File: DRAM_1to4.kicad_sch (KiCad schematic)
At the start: 1 part, among them U1 K4A8G085WC-BCPB

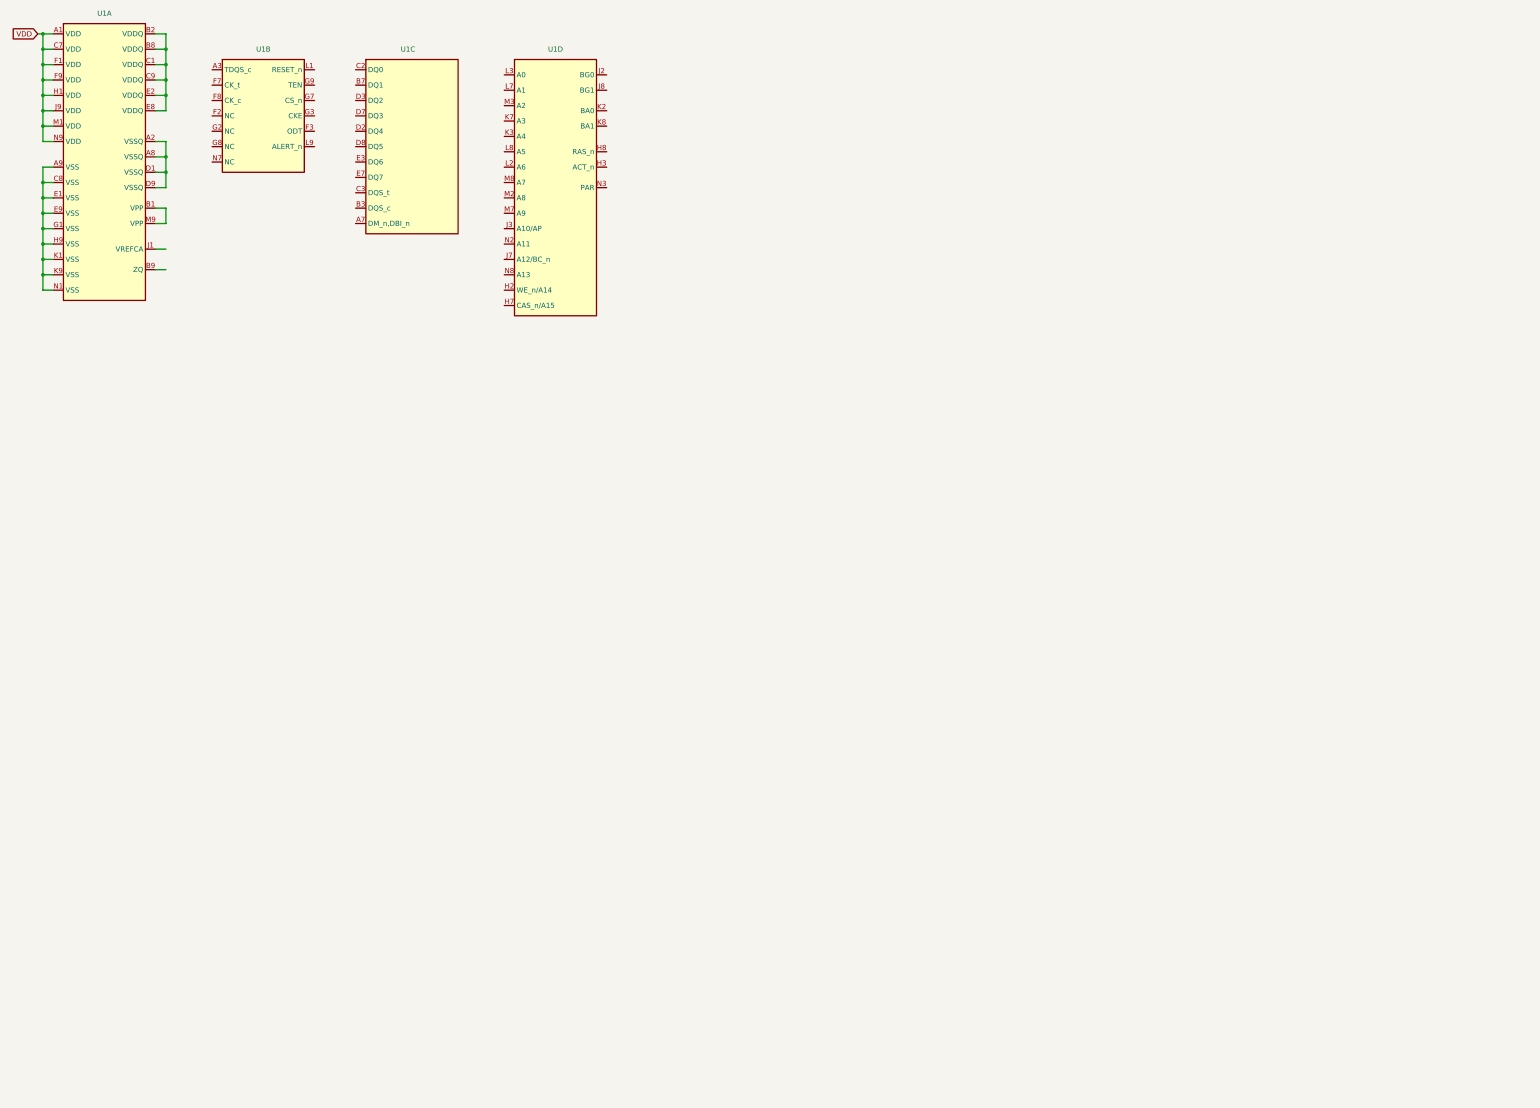
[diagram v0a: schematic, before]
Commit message: Update schametic 1. Adding 7 DRAMS, 2. Replacing a SPD EEPROM with new one that is including in a temperature sensor, 3. modifying a DIMM Connector and DRAM PAD
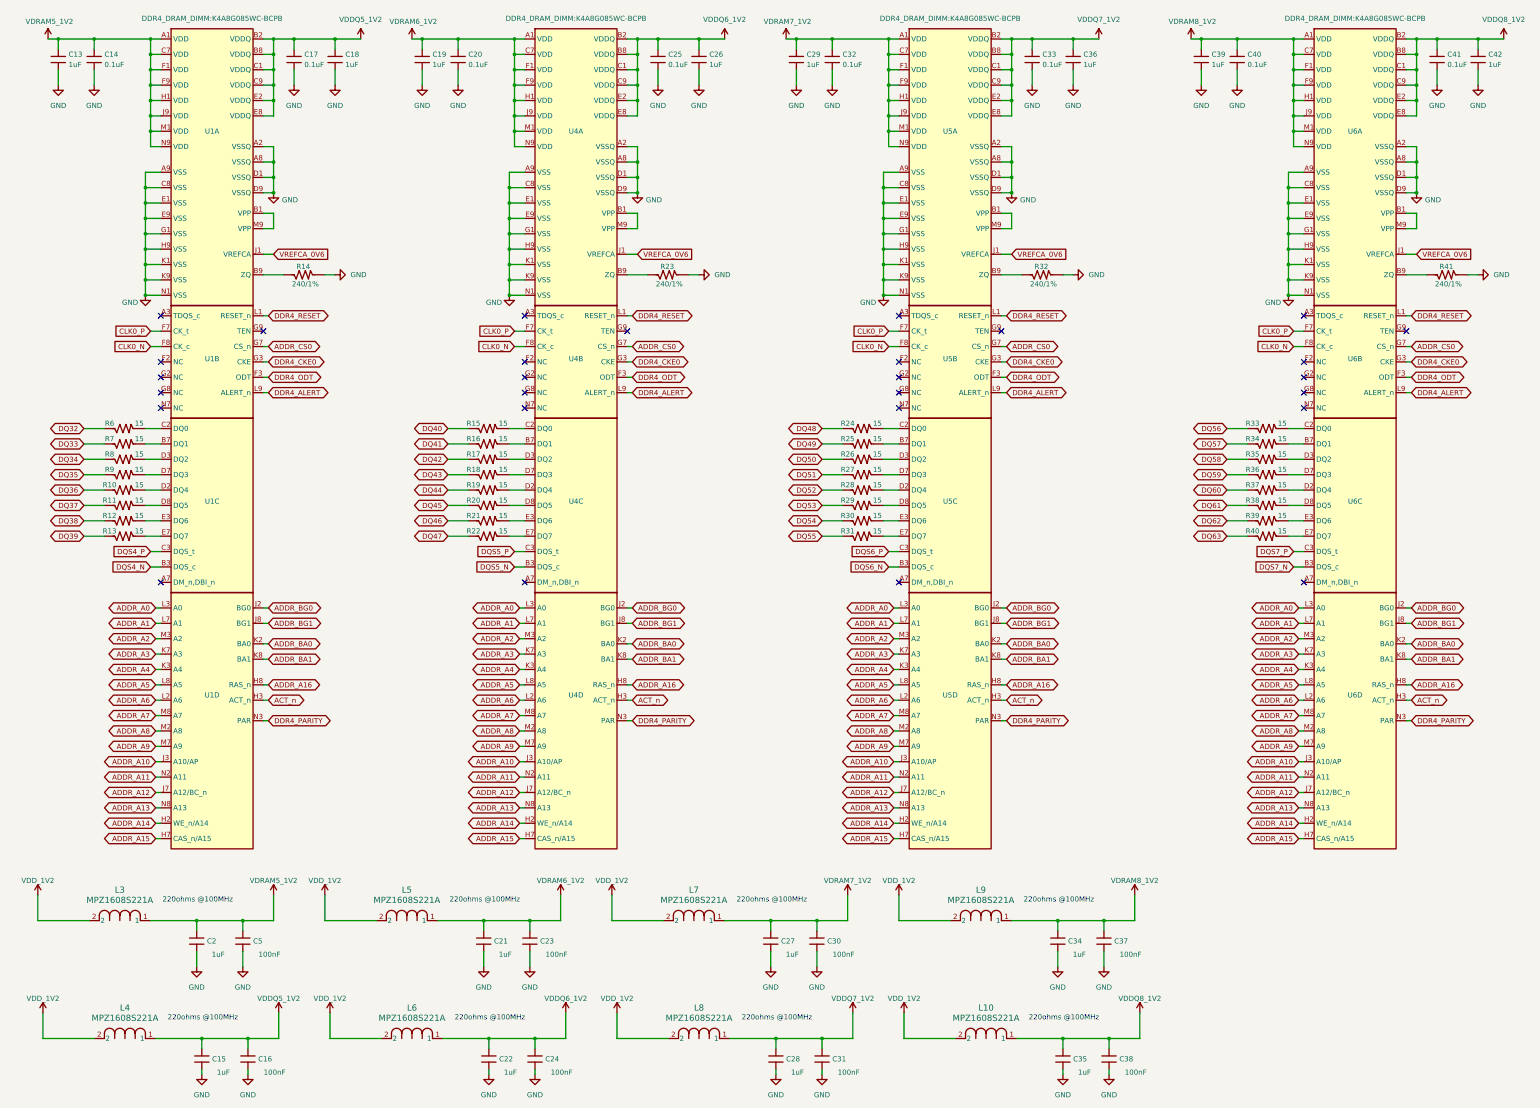
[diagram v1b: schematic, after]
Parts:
- removed U1: K4A8G085WC-BCPB, DDR4_DRAM_DIMM:K4A8G085WC-BCPB, symbol DDR4_DRAM_DIMM:K4A8G085WC-BCPB
- added C13, C18, C19, C26, C29, C36, C39, C42: 1uF, Capacitor_SMD:C_0402_1005Metric_Pad0.74x0.62mm_HandSolder, symbol Mixed_signal:CAP_1608
- added C14, C17, C20, C25, C32, C33, C40, C41: 0.1uF, Capacitor_SMD:C_0402_1005Metric_Pad0.74x0.62mm_HandSolder, symbol Mixed_signal:CAP_1608
- added C15, C2, C21, C22, C27, C28, C34, C35: 1uF, Capacitor_SMD:C_01005_0402Metric_Pad0.57x0.30mm_HandSolder, symbol Mixed_signal:CAP_1005
- added C16, C23, C24, C30, C31, C37, C38, C5: 100nF, Capacitor_SMD:C_01005_0402Metric_Pad0.57x0.30mm_HandSolder, symbol Mixed_signal:CAP_1005
- added L10, L3, L4, L5, L6, L7, L8, L9: MPZ1608S221A, DDR4_DRAM_DIMM:MPZ1608S260ATAH0, symbol MPZ1608S260ATAH0:MPZ1608S221A
- added R10, R11, R12, R13, R15, R16, R17, R18, R19, R20, R21, R22, R24, R25, R26, R27, R28, R29, R30, R31, R33, R34, R35, R36, R37, R38, R39, R40, R6, R7, R8, R9: 15, Capacitor_SMD:C_0402_1005Metric_Pad0.74x0.62mm_HandSolder, symbol Mixed_signal:RES_1005
- added R14, R23, R32, R41: 240/1%, Capacitor_SMD:C_0402_1005Metric_Pad0.74x0.62mm_HandSolder, symbol Mixed_signal:RES_1005
- added U1, U4, U5, U6: K4A8G085WC-BCPB, DDR4_DRAM_DIMM:K4A8G085WC-BCPB, symbol DDR4_DIMM:K4A8G085WC-BCPB
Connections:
- new net: R7.2, U1.B7 (DQ1)
- new net: R6.2, U1.C2 (DQ0)
- new net: R10.2, U1.D2 (DQ4)
- new net: R8.2, U1.D3 (DQ2)
- new net: R9.2, U1.D7 (DQ3)
- new net: R11.2, U1.D8 (DQ5)
- new net: R12.2, U1.E3 (DQ6)
- new net: R13.2, U1.E7 (DQ7)
- new net: R16.2, U4.B7 (DQ1)
- new net: R29.2, U5.D8 (DQ5)
- new net: R27.2, U5.D7 (DQ3)
- new net: R34.2, U6.B7 (DQ1)
- new net: R18.2, U4.D7 (DQ3)
- new net: U1.B1 (VPP), U1.M9 (VPP)
- new net: R14.1, U1.B9 (ZQ)
- new net: R39.2, U6.E3 (DQ6)
- new net: R40.2, U6.E7 (DQ7)
- new net: R26.2, U5.D3 (DQ2)
- new net: R19.2, U4.D2 (DQ4)
- new net: R24.2, U5.C2 (DQ0)
- new net: R25.2, U5.B7 (DQ1)
- new net: R28.2, U5.D2 (DQ4)
- new net: R30.2, U5.E3 (DQ6)
- new net: R31.2, U5.E7 (DQ7)
- new net: R32.1, U5.B9 (ZQ)
- new net: R37.2, U6.D2 (DQ4)
- new net: R15.2, U4.C2 (DQ0)
- new net: R17.2, U4.D3 (DQ2)
- new net: R20.2, U4.D8 (DQ5)
- new net: R21.2, U4.E3 (DQ6)
- new net: R22.2, U4.E7 (DQ7)
- new net: U5.B1 (VPP), U5.M9 (VPP)
- new net: R38.2, U6.D8 (DQ5)
- new net: R35.2, U6.D3 (DQ2)
- new net: R41.1, U6.B9 (ZQ)
- new net: R33.2, U6.C2 (DQ0)
- new net: R23.1, U4.B9 (ZQ)
- new net: R36.2, U6.D7 (DQ3)
- new net: U4.B1 (VPP), U4.M9 (VPP)
- new net: U6.B1 (VPP), U6.M9 (VPP)
- new net ACT_n: U1.H3 (ACT_n), U4.H3 (ACT_n), U5.H3 (ACT_n), U6.H3 (ACT_n)
- new net ADDR_A0: U1.L3 (A0), U4.L3 (A0), U5.L3 (A0), U6.L3 (A0)
- new net ADDR_A1: U1.L7 (A1), U4.L7 (A1), U5.L7 (A1), U6.L7 (A1)
- new net ADDR_A10: U1.J3 (A10/AP), U4.J3 (A10/AP), U5.J3 (A10/AP), U6.J3 (A10/AP)
- new net ADDR_A11: U1.N2 (A11), U4.N2 (A11), U5.N2 (A11), U6.N2 (A11)
- new net ADDR_A12: U1.J7 (A12/BC_n), U4.J7 (A12/BC_n), U5.J7 (A12/BC_n), U6.J7 (A12/BC_n)
- new net ADDR_A13: U1.N8 (A13), U4.N8 (A13), U5.N8 (A13), U6.N8 (A13)
- new net ADDR_A14: U1.H2 (WE_n/A14), U4.H2 (WE_n/A14), U5.H2 (WE_n/A14), U6.H2 (WE_n/A14)
- new net ADDR_A15: U1.H7 (CAS_n/A15), U4.H7 (CAS_n/A15), U5.H7 (CAS_n/A15), U6.H7 (CAS_n/A15)
- new net ADDR_A16: U1.H8 (RAS_n), U4.H8 (RAS_n), U5.H8 (RAS_n), U6.H8 (RAS_n)
- new net ADDR_A2: U1.M3 (A2), U4.M3 (A2), U5.M3 (A2), U6.M3 (A2)
- new net ADDR_A3: U1.K7 (A3), U4.K7 (A3), U5.K7 (A3), U6.K7 (A3)
- new net ADDR_A4: U1.K3 (A4), U4.K3 (A4), U5.K3 (A4), U6.K3 (A4)
- new net ADDR_A5: U1.L8 (A5), U4.L8 (A5), U5.L8 (A5), U6.L8 (A5)
- new net ADDR_A6: U1.L2 (A6), U4.L2 (A6), U5.L2 (A6), U6.L2 (A6)
- new net ADDR_A7: U1.M8 (A7), U4.M8 (A7), U5.M8 (A7), U6.M8 (A7)
- new net ADDR_A8: U1.M2 (A8), U4.M2 (A8), U5.M2 (A8), U6.M2 (A8)
- new net ADDR_A9: U1.M7 (A9), U4.M7 (A9), U5.M7 (A9), U6.M7 (A9)
- new net ADDR_BA0: U1.K2 (BA0), U4.K2 (BA0), U5.K2 (BA0), U6.K2 (BA0)
- new net ADDR_BA1: U1.K8 (BA1), U4.K8 (BA1), U5.K8 (BA1), U6.K8 (BA1)
- new net ADDR_BG0: U1.J2 (BG0), U4.J2 (BG0), U5.J2 (BG0), U6.J2 (BG0)
- new net ADDR_BG1: U1.J8 (BG1), U4.J8 (BG1), U5.J8 (BG1), U6.J8 (BG1)
- new net ADDR_CS0: U1.G7 (CS_n), U4.G7 (CS_n), U5.G7 (CS_n), U6.G7 (CS_n)
- new net CLK0_N: U1.F8 (CK_c), U4.F8 (CK_c), U5.F8 (CK_c), U6.F8 (CK_c)
- new net CLK0_P: U1.F7 (CK_t), U4.F7 (CK_t), U5.F7 (CK_t), U6.F7 (CK_t)
- new net DDR4_ALERT: U1.L9 (ALERT_n), U4.L9 (ALERT_n), U5.L9 (ALERT_n), U6.L9 (ALERT_n)
- new net DDR4_CKE0: U1.G3 (CKE), U4.G3 (CKE), U5.G3 (CKE), U6.G3 (CKE)
- new net DDR4_ODT: U1.F3 (ODT), U4.F3 (ODT), U5.F3 (ODT), U6.F3 (ODT)
- new net DDR4_PARITY: U1.N3 (PAR), U4.N3 (PAR), U5.N3 (PAR), U6.N3 (PAR)
- new net DDR4_RESET: U1.L1 (RESET_n), U4.L1 (RESET_n), U5.L1 (RESET_n), U6.L1 (RESET_n)
- new net DQ32: R6.1
- new net DQ33: R7.1
- new net DQ34: R8.1
- new net DQ35: R9.1
- new net DQ36: R10.1
- new net DQ37: R11.1
- new net DQ38: R12.1
- new net DQ39: R13.1
- new net DQ40: R15.1
- new net DQ41: R16.1
- new net DQ42: R17.1
- new net DQ43: R18.1
- new net DQ44: R19.1
- new net DQ45: R20.1
- new net DQ46: R21.1
- new net DQ47: R22.1
- new net DQ48: R24.1
- new net DQ49: R25.1
- new net DQ50: R26.1
- new net DQ51: R27.1
- new net DQ52: R28.1
- new net DQ53: R29.1
- new net DQ54: R30.1
- new net DQ55: R31.1
- new net DQ56: R33.1
- new net DQ57: R34.1
- new net DQ58: R35.1
- new net DQ59: R36.1
- new net DQ60: R37.1
- new net DQ61: R38.1
- new net DQ62: R39.1
- new net DQ63: R40.1
- new net DQS4_N: U1.B3 (DQS_c)
- new net DQS4_P: U1.C3 (DQS_t)
- new net DQS5_N: U4.B3 (DQS_c)
- new net DQS5_P: U4.C3 (DQS_t)
- new net DQS6_N: U5.B3 (DQS_c)
- new net DQS6_P: U5.C3 (DQS_t)
- new net DQS7_N: U6.B3 (DQS_c)
- new net DQS7_P: U6.C3 (DQS_t)
- new net GND: C13.1, C14.1, C15.1, C16.1, C17.1, C18.1, C19.1, C2.1, C20.1, C21.1, C22.1, C23.1, C24.1, C25.1, C26.1, C27.1, C28.1, C29.1, C30.1, C31.1, C32.1, C33.1, C34.1, C35.1, C36.1, C37.1, C38.1, C39.1, C40.1, C41.1, C42.1, C5.1, R14.2, R23.2, R32.2, R41.2, U1.A2 (VSSQ), U1.A8 (VSSQ), U1.A9 (VSS), U1.C8 (VSS), U1.D1 (VSSQ), U1.D9 (VSSQ), U1.E1 (VSS), U1.E9 (VSS), U1.G1 (VSS), U1.H9 (VSS), U1.K1 (VSS), U1.K9 (VSS), U1.N1 (VSS), U4.A2 (VSSQ), U4.A8 (VSSQ), U4.A9 (VSS), U4.C8 (VSS), U4.D1 (VSSQ), U4.D9 (VSSQ), U4.E1 (VSS), U4.E9 (VSS), U4.G1 (VSS), U4.H9 (VSS), U4.K1 (VSS), U4.K9 (VSS), U4.N1 (VSS), U5.A2 (VSSQ), U5.A8 (VSSQ), U5.A9 (VSS), U5.C8 (VSS), U5.D1 (VSSQ), U5.D9 (VSSQ), U5.E1 (VSS), U5.E9 (VSS), U5.G1 (VSS), U5.H9 (VSS), U5.K1 (VSS), U5.K9 (VSS), U5.N1 (VSS), U6.A2 (VSSQ), U6.A8 (VSSQ), U6.A9 (VSS), U6.C8 (VSS), U6.D1 (VSSQ), U6.D9 (VSSQ), U6.E1 (VSS), U6.E9 (VSS), U6.G1 (VSS), U6.H9 (VSS), U6.K1 (VSS), U6.K9 (VSS), U6.N1 (VSS)
- new net VDDQ5_1V2: C15.2, C16.2, C17.2, C18.2, L4.1, U1.B2 (VDDQ), U1.B8 (VDDQ), U1.C1 (VDDQ), U1.C9 (VDDQ), U1.E2 (VDDQ), U1.E8 (VDDQ)
- new net VDDQ6_1V2: C22.2, C24.2, C25.2, C26.2, L6.1, U4.B2 (VDDQ), U4.B8 (VDDQ), U4.C1 (VDDQ), U4.C9 (VDDQ), U4.E2 (VDDQ), U4.E8 (VDDQ)
- new net VDDQ7_1V2: C28.2, C31.2, C33.2, C36.2, L8.1, U5.B2 (VDDQ), U5.B8 (VDDQ), U5.C1 (VDDQ), U5.C9 (VDDQ), U5.E2 (VDDQ), U5.E8 (VDDQ)
- new net VDDQ8_1V2: C35.2, C38.2, C41.2, C42.2, L10.1, U6.B2 (VDDQ), U6.B8 (VDDQ), U6.C1 (VDDQ), U6.C9 (VDDQ), U6.E2 (VDDQ), U6.E8 (VDDQ)
- new net VDD_1V2: L10.2, L3.2, L4.2, L5.2, L6.2, L7.2, L8.2, L9.2
- new net VDRAM5_1V2: C13.2, C14.2, C2.2, C5.2, L3.1, U1.A1 (VDD), U1.C7 (VDD), U1.F1 (VDD), U1.F9 (VDD), U1.H1 (VDD), U1.J9 (VDD), U1.M1 (VDD), U1.N9 (VDD)
- new net VDRAM6_1V2: C19.2, C20.2, C21.2, C23.2, L5.1, U4.A1 (VDD), U4.C7 (VDD), U4.F1 (VDD), U4.F9 (VDD), U4.H1 (VDD), U4.J9 (VDD), U4.M1 (VDD), U4.N9 (VDD)
- new net VDRAM7_1V2: C27.2, C29.2, C30.2, C32.2, L7.1, U5.A1 (VDD), U5.C7 (VDD), U5.F1 (VDD), U5.F9 (VDD), U5.H1 (VDD), U5.J9 (VDD), U5.M1 (VDD), U5.N9 (VDD)
- new net VDRAM8_1V2: C34.2, C37.2, C39.2, C40.2, L9.1, U6.A1 (VDD), U6.C7 (VDD), U6.F1 (VDD), U6.F9 (VDD), U6.H1 (VDD), U6.J9 (VDD), U6.M1 (VDD), U6.N9 (VDD)
- new net VREFCA_0V6: U1.J1 (VREFCA), U4.J1 (VREFCA), U5.J1 (VREFCA), U6.J1 (VREFCA)
- no-connect marks 0 -> 28
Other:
- note added: "220ohms @100MHz"
